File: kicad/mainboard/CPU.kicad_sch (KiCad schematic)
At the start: 23 parts, among them J12 Conn 02x03, J13 Conn_02x12, J3 RADIO INTERFACE, J9 LINK INPUT, U1 ATMEGA16/32-P, U9 MAX232

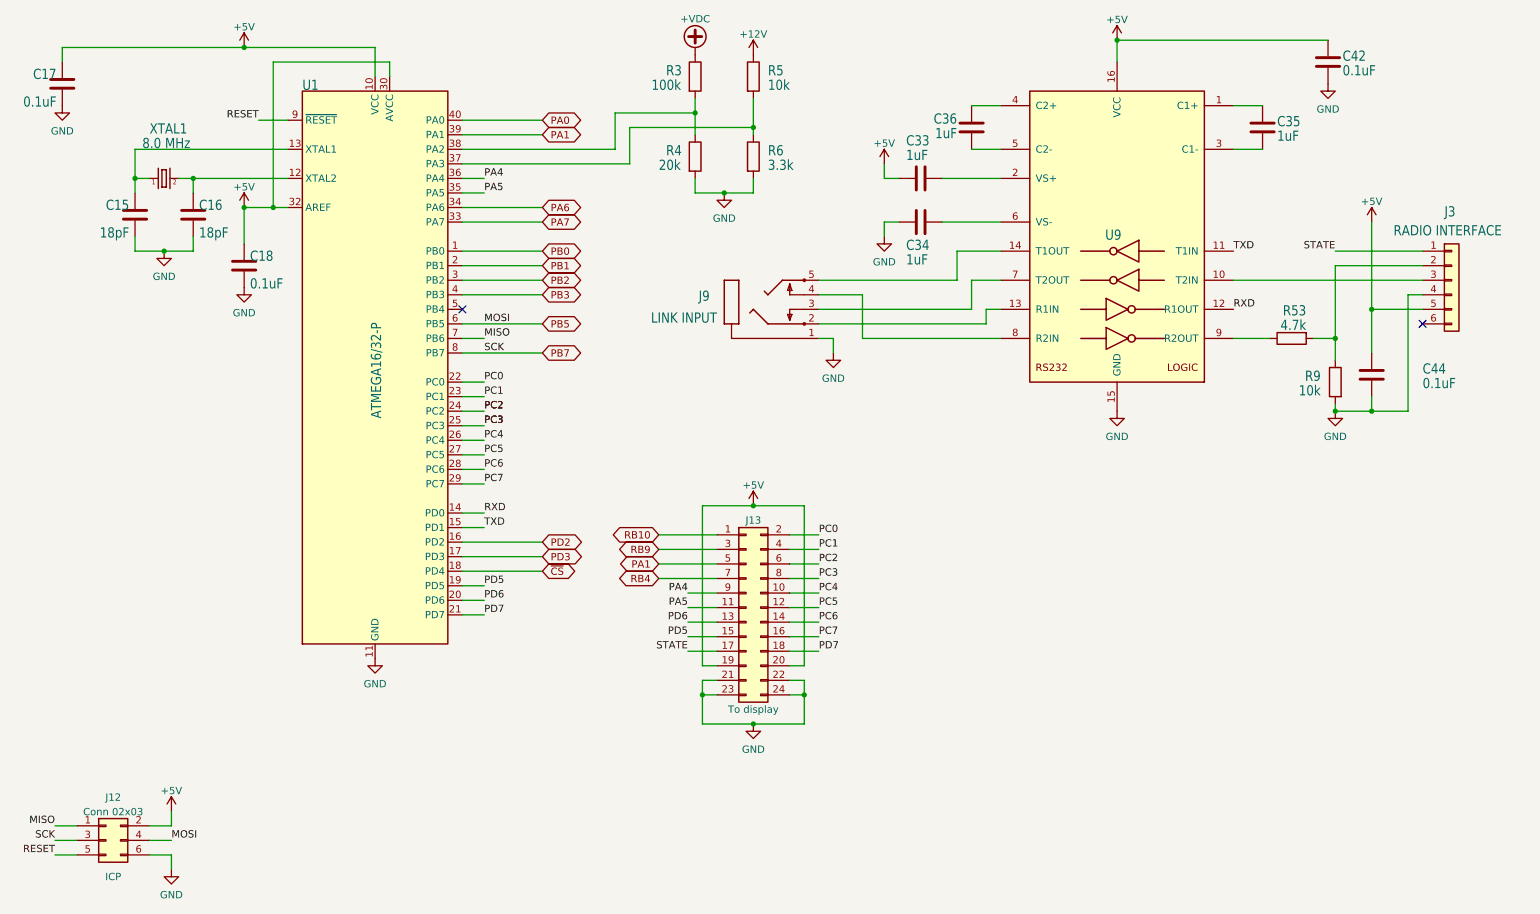
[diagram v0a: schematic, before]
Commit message: Bringing mainboard up to par with V1.4 schematics based on images. Rerouted a few lines since they could not pass below the MOSFETs due to a different footprint/pad size.
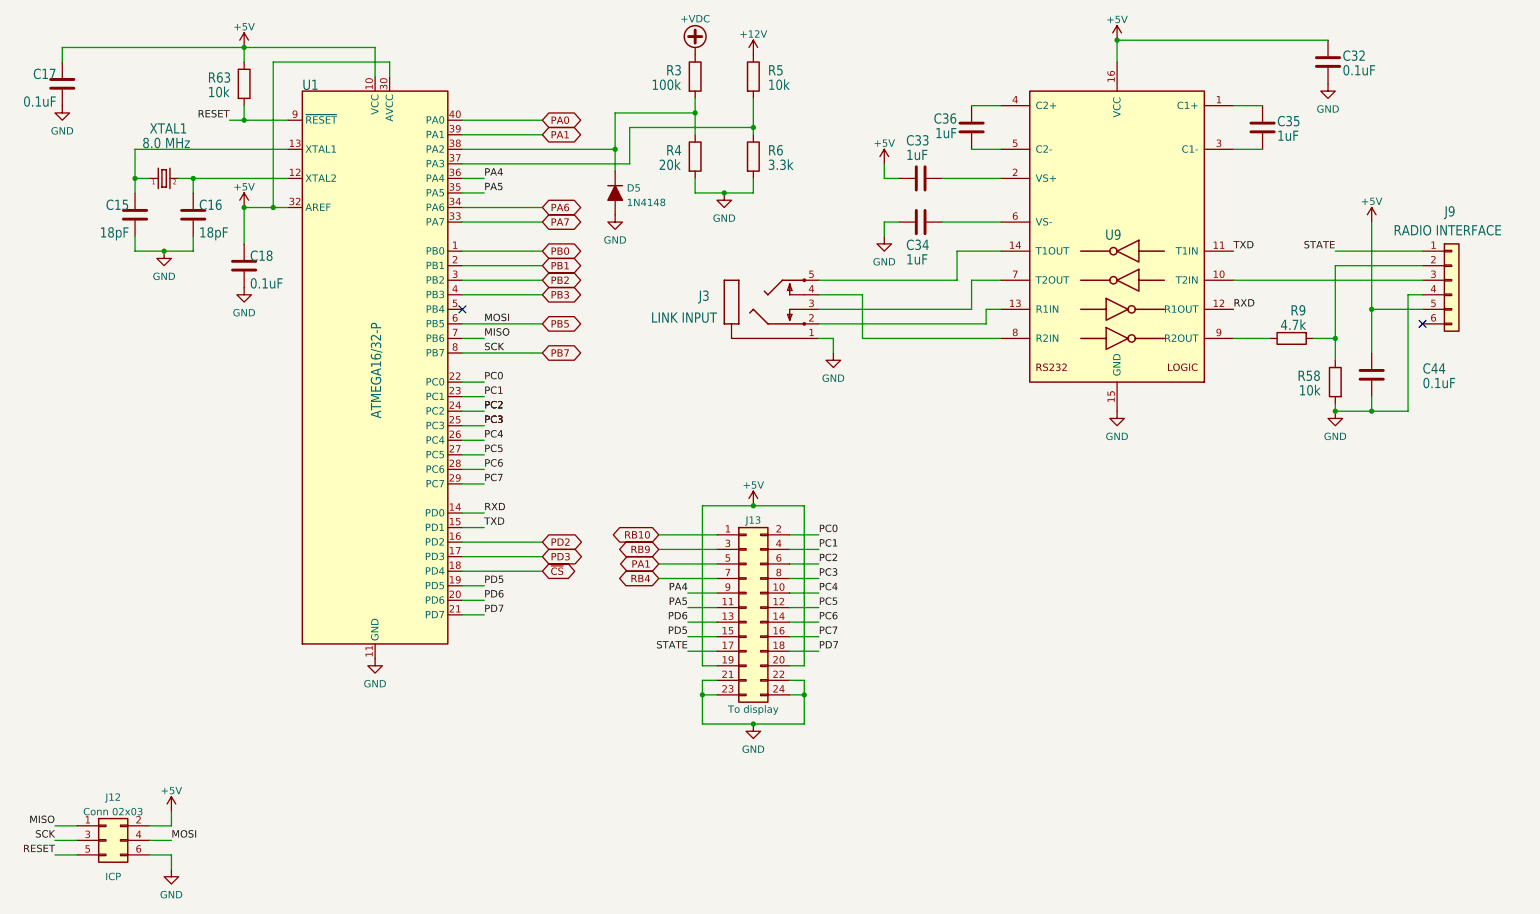
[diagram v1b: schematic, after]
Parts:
- added D5: 1N4148, Diode_THT:D_DO-35_SOD27_P10.16mm_Horizontal, symbol Device:D_Filled
- added R63: 10k, Resistor_THT:R_Axial_DIN0207_L6.3mm_D2.5mm_P10.16mm_Horizontal, symbol Device:R
- renumbered C42 to C32, J9 to J3, J3 to J9, R9 to R58, R53 to R9
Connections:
- net +5V: now also R63.1
- net GND: now also D5.2 (A)
- net RESET: now also R63.2
- net at R3.2, R4.1, U1.38 (PA2): now also D5.1 (K)
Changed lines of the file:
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@@
   (junction (at 259.08 77.47) (diameter 0) (color 0 0 0 0)
   )
+  (junction (at 127 49.53) (diameter 0) (color 0 0 0 0)
+  )
   (junction (at 151.13 149.86) (diameter 0) (color 0 0 0 0)
   )
@@
   )
   (junction (at 62.23 59.69) (diameter 0) (color 0 0 0 0)
+  )
+  (junction (at 62.23 44.45) (diameter 0) (color 0 0 0 0)
   )
   (junction (at 53.34 54.61) (diameter 0) (color 0 0 0 0)
@@
     (stroke (width 0) (type default) (color 0 0 0 0))
   )
-  (wire (pts (xy 69.85 44.45) (xy 64.77 44.45))
+  (wire (pts (xy 59.69 44.45) (xy 62.23 44.45))
     (stroke (width 0) (type default) (color 0 0 0 0))
   )
@@
     (stroke (width 0) (type default) (color 0 0 0 0))
   )
+  (wire (pts (xy 62.23 44.45) (xy 69.85 44.45))
+    (stroke (width 0) (type default) (color 0 0 0 0))
+  )
   (wire (pts (xy 140.97 54.61) (xy 140.97 57.15))
     (stroke (width 0) (type default) (color 0 0 0 0))
@@
     (stroke (width 0) (type default) (color 0 0 0 0))
   )
+  (wire (pts (xy 62.23 41.91) (xy 62.23 44.45))
+    (stroke (width 0) (type default) (color 0 0 0 0))
+  )
   (wire (pts (xy 157.48 124.46) (xy 162.56 124.46))
     (stroke (width 0) (type default) (color 0 0 0 0))
@@
     (stroke (width 0) (type default) (color 0 0 0 0))
   )
+  (wire (pts (xy 62.23 31.75) (xy 62.23 34.29))
+    (stroke (width 0) (type default) (color 0 0 0 0))
+  )
   (wire (pts (xy 127 49.53) (xy 127 43.18))
     (stroke (width 0) (type default) (color 0 0 0 0))
@@
   )
   (wire (pts (xy 234.95 41.91) (xy 240.03 41.91))
+    (stroke (width 0) (type default) (color 0 0 0 0))
+  )
+  (wire (pts (xy 127 49.53) (xy 127 53.34))
     (stroke (width 0) (type default) (color 0 0 0 0))
   )
@@
     (effects (font (size 1.27 1.27)) (justify left bottom))
   )
-  (label "RESET" (at 64.77 44.45 180)
+  (label "RESET" (at 59.69 44.45 180)
     (effects (font (size 1.27 1.27)) (justify right bottom))
   )
@@
     )
     (pin "1")
+  )
+  (symbol (lib_id "Device:D_Filled") (at 127 57.15 270) (unit 1)
+    (in_bom yes) (on_board yes) (fields_autoplaced)
+    (property "Reference" "D5" (id 0) (at 129.032 56.3153 90)
+      (effects (font (size 1.27 1.27)) (justify left))
+    )
+    (property "Value" "1N4148" (id 1) (at 129.032 58.8522 90)
+      (effects (font (size 1.27 1.27)) (justify left))
+    )
+    (property "Footprint" "Diode_THT:D_DO-35_SOD27_P10.16mm_Horizontal" (id 2) (at 127 57.15 0)
+      (effects (font (size 1.27 1.27)) hide)
+    )
+    (property "Datasheet" "~" (id 3) (at 127 57.15 0)
+      (effects (font (size 1.27 1.27)) hide)
+    )
+    (pin "1")
+    (pin "2")
   )
   (symbol (lib_id "Device:R") (at 140.97 50.8 0) (unit 1)
@@
   (symbol (lib_id "Device:R") (at 252.73 90.17 0) (mirror y) (unit 1)
     (in_bom yes) (on_board yes)
-    (property "Reference" "R9" (id 0) (at 250.19 90.17 0)
+    (property "Reference" "R58" (id 0) (at 250.19 90.17 0)
       (effects (font (size 1.778 1.5113)) (justify left bottom))
     )
@@
     )
     (property "Datasheet" "~" (id 3) (at 252.73 90.17 0)
+      (effects (font (size 1.27 1.27)) hide)
+    )
+    (pin "1")
+    (pin "2")
+  )
+  (symbol (lib_id "Device:R") (at 62.23 38.1 0) (unit 1)
+    (in_bom yes) (on_board yes)
+    (property "Reference" "R63" (id 0) (at 55.88 38.1 0)
+      (effects (font (size 1.778 1.5113)) (justify left bottom))
+    )
+    (property "Value" "10k" (id 1) (at 55.88 40.64 0)
+      (effects (font (size 1.778 1.5113)) (justify left bottom))
+    )
+    (property "Footprint" "Resistor_THT:R_Axial_DIN0207_L6.3mm_D2.5mm_P10.16mm_Horizontal" (id 2) (at 60.452 38.1 90)
+      (effects (font (size 1.27 1.27)) hide)
+    )
+    (property "Datasheet" "~" (id 3) (at 62.23 38.1 0)
       (effects (font (size 1.27 1.27)) hide)
     )
@@
   (symbol (lib_id "Device:R") (at 245.11 82.55 90) (mirror x) (unit 1)
     (in_bom yes) (on_board yes)
-    (property "Reference" "R53" (id 0) (at 247.65 78.74 90)
+    (property "Reference" "R9" (id 0) (at 247.65 78.74 90)
       (effects (font (size 1.778 1.5113)) (justify left bottom))
     )
@@
   (symbol (lib_id "Connector_Generic:Conn_01x06") (at 273.05 72.39 0) (unit 1)
     (in_bom yes) (on_board yes)
-    (property "Reference" "J3" (id 0) (at 271.78 61.468 0)
+    (property "Reference" "J9" (id 0) (at 271.78 61.468 0)
       (effects (font (size 1.778 1.5113)) (justify left bottom))
     )
@@
   (symbol (lib_id "mk312-eagle-import:STEREOJACK") (at 149.86 74.93 0) (mirror y) (unit 1)
     (in_bom yes) (on_board yes)
-    (property "Reference" "J9" (id 0) (at 143.51 76.2 0)
+    (property "Reference" "J3" (id 0) (at 143.51 76.2 0)
       (effects (font (size 1.778 1.5113)) (justify left bottom))
     )
@@
   (symbol (lib_id "Device:C") (at 251.46 34.29 0) (unit 1)
     (in_bom yes) (on_board yes)
-    (property "Reference" "C42" (id 0) (at 254 34.29 0)
+    (property "Reference" "C32" (id 0) (at 254 34.29 0)
       (effects (font (size 1.778 1.5113)) (justify left bottom))
     )
@@
     (pin "2")
   )
+  (symbol (lib_id "power:GND") (at 127 60.96 0) (unit 1)
+    (in_bom yes) (on_board yes) (fields_autoplaced)
+    (property "Reference" "#PWR03" (id 0) (at 127 67.31 0)
+      (effects (font (size 1.27 1.27)) hide)
+    )
+    (property "Value" "GND" (id 1) (at 127 65.4034 0))
+    (property "Footprint" "" (id 2) (at 127 60.96 0)
+      (effects (font (size 1.27 1.27)) hide)
+    )
+    (property "Datasheet" "" (id 3) (at 127 60.96 0)
+      (effects (font (size 1.27 1.27)) hide)
+    )
+    (pin "1")
+  )
   (symbol (lib_id "Device:R") (at 151.13 50.8 0) (unit 1)

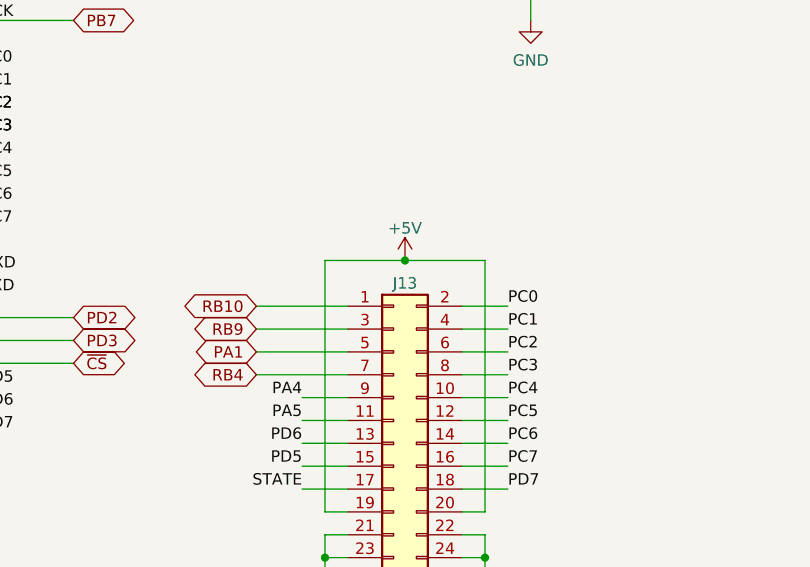
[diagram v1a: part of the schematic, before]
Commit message: Brought component numbers back in line with the original schematics
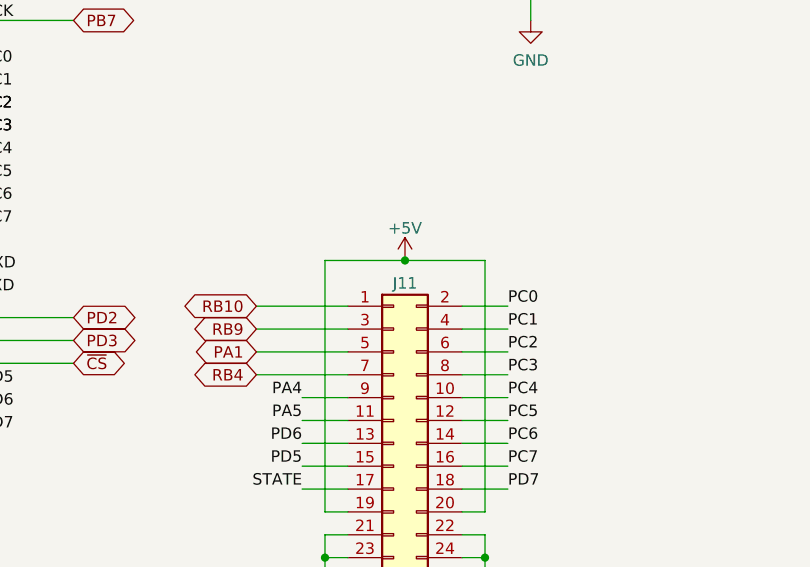
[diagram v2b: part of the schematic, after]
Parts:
- renumbered J13 to J11
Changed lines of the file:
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@@
   (symbol (lib_id "Connector_Generic:Conn_02x12_Odd_Even") (at 149.86 129.54 0) (unit 1)
     (in_bom yes) (on_board yes)
-    (property "Reference" "J13" (id 0) (at 151.13 114.3 0))
+    (property "Reference" "J11" (id 0) (at 151.13 114.3 0))
     (property "Value" "Conn_02x12" (id 1) (at 149.86 105.41 0)
       (effects (font (size 1.27 1.27)) hide)
